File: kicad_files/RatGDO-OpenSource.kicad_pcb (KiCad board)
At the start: 2 copper layers, 55 x 70 mm, 15 parts, among them J1 Screw_Terminal_01x03, J2 Screw_Terminal_01x03, Q1 2N7002, Q2 AO3400A, U1 WeMos_D1_mini, U2 AMS1117-3.3

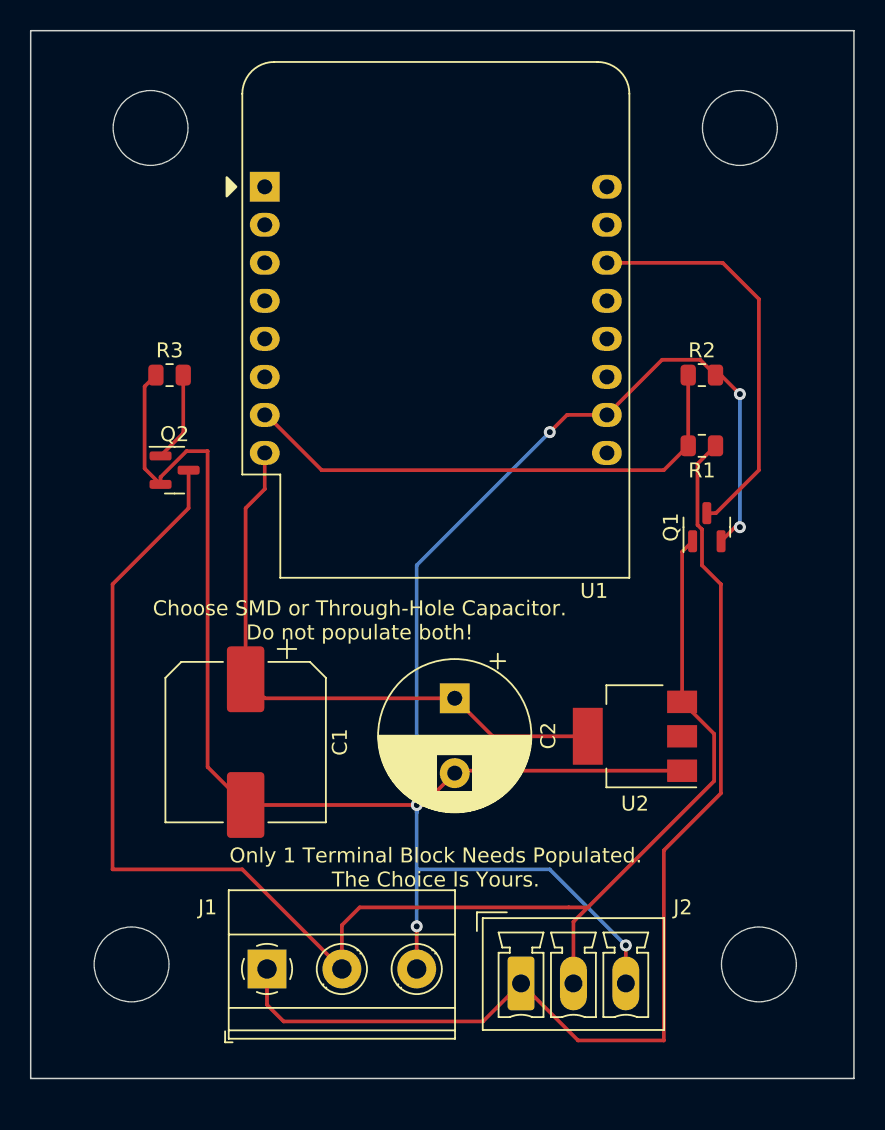
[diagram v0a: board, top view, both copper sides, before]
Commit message: Updated Files to match new Schematics
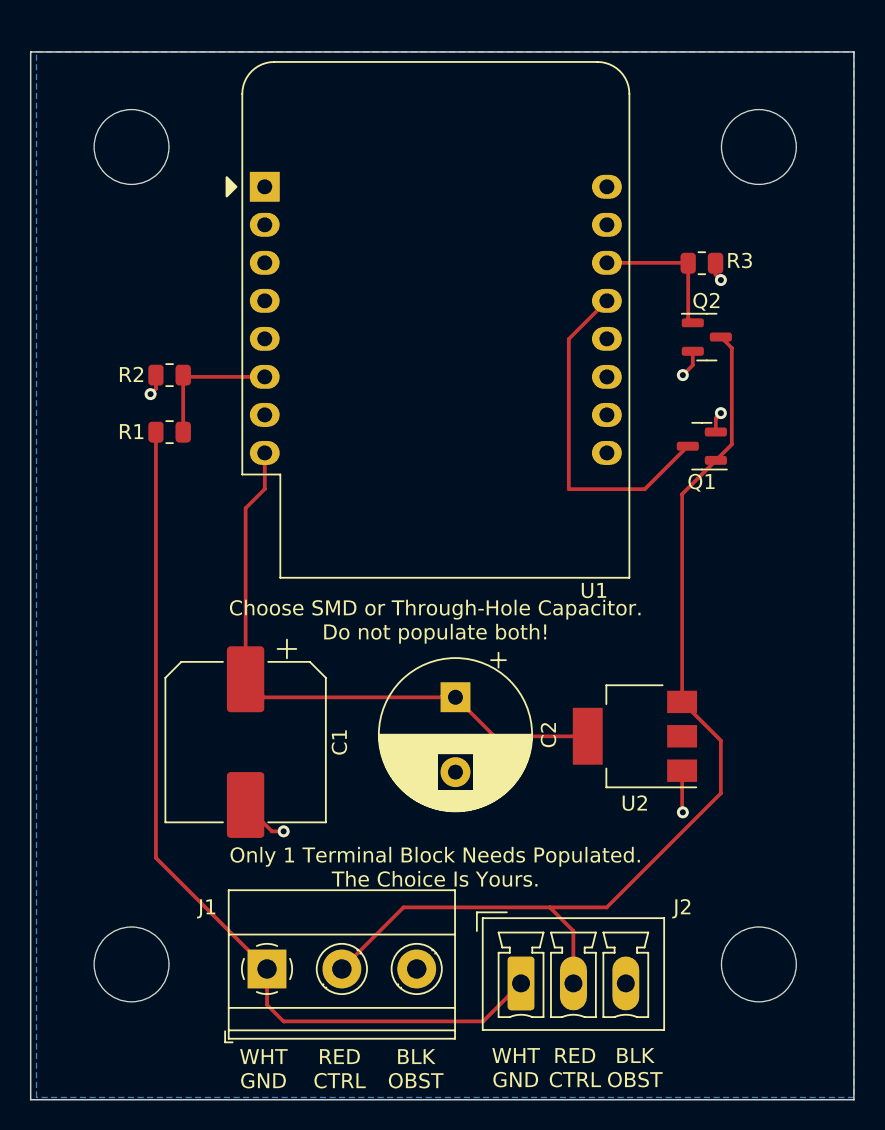
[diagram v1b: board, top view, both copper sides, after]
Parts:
- moved Q2 36.7 mm to (159.1, 76.2)
- moved R3 36.3 mm to (158.8, 71.3), turned to 180 degrees
- moved R1 35.6 mm to (123.2, 82.5), turned to 0 degrees
- moved R2 35.6 mm to (123.2, 78.7), turned to 180 degrees
- moved Q1 5.42 mm to (158.8, 83.5), turned to 180 degrees
- moved REF** 1.80 mm to (162.6, 63.5)
- moved REF** 1.80 mm to (120.7, 63.5)
- moved C2 0.08 mm to (142.3, 100.3)
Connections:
- R1 pad 2: Net-(U1-CS/D8) -> Net-(U1-MOSI/D7)
- R2 pad 1: Net-(U1-CS/D8) -> Net-(U1-MOSI/D7)
- U1 pad 13: unconnected-(U1-SDA/D2-Pad13) -> Net-(Q1-D)
- U1 pad 14: Net-(Q1-D) -> Net-(Q2-G)
- U1 pad 6: unconnected-(U1-MOSI/D7-Pad6) -> Net-(U1-MOSI/D7)
- U1 pad 7: Net-(U1-CS/D8) -> unconnected-(U1-CS/D8-Pad7)
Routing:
- net GND: track 152.0 -> 12.2 mm
- net Net-(U1-CS/D8): track 35.2 -> 0.00 mm
- net Net-(J1-Pin_2): track 101.3 -> 69.1 mm
- net Net-(J1-Pin_1): track 74.4 -> 59.8 mm
- net Net-(U1-MOSI/D7): track 0.00 -> 9.30 mm
- net Net-(Q1-D): track 27.3 -> 22.8 mm
- net Net-(Q2-G): track 6.03 -> 9.55 mm
- added copper zone on B.Cu, net GND
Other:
- board text added: "BLK OBST"
- board text added: "RED CTRL"
- board text added: "WHT GND"

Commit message: Remove power supply components
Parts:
- removed C1: 16v1000uf, Capacitor_SMD:CP_Elec_10x10.5
- removed C2: 16v1000uf, Capacitor_THT:CP_Radial_D10.0mm_P5.00mm
- removed U2: AMS1117-3.3, Package_TO_SOT_SMD:SOT-223-3_TabPin2
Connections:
- U1 pad 8: VCC -> +3.3V
- U1 pad 9: unconnected-(U1-5V-Pad9) -> +5V
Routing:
- net VCC: track 40.2 -> 0.00 mm
- net Net-(Q1-D): track 22.8 -> 11.9 mm
- net GND: track 12.2 -> 5.95 mm, vias 6 -> 4
- net Net-(J1-Pin_2): track 69.1 -> 67.0 mm
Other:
- board text removed: "Choose SMD or Through-Hole Capacitor. Do not populate both!"
